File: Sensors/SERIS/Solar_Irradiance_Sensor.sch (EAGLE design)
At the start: 7 parts, among them IC1 LM324N, J1 ARDUINO_R3_SHIELD, U1 V_REG_317DPACK

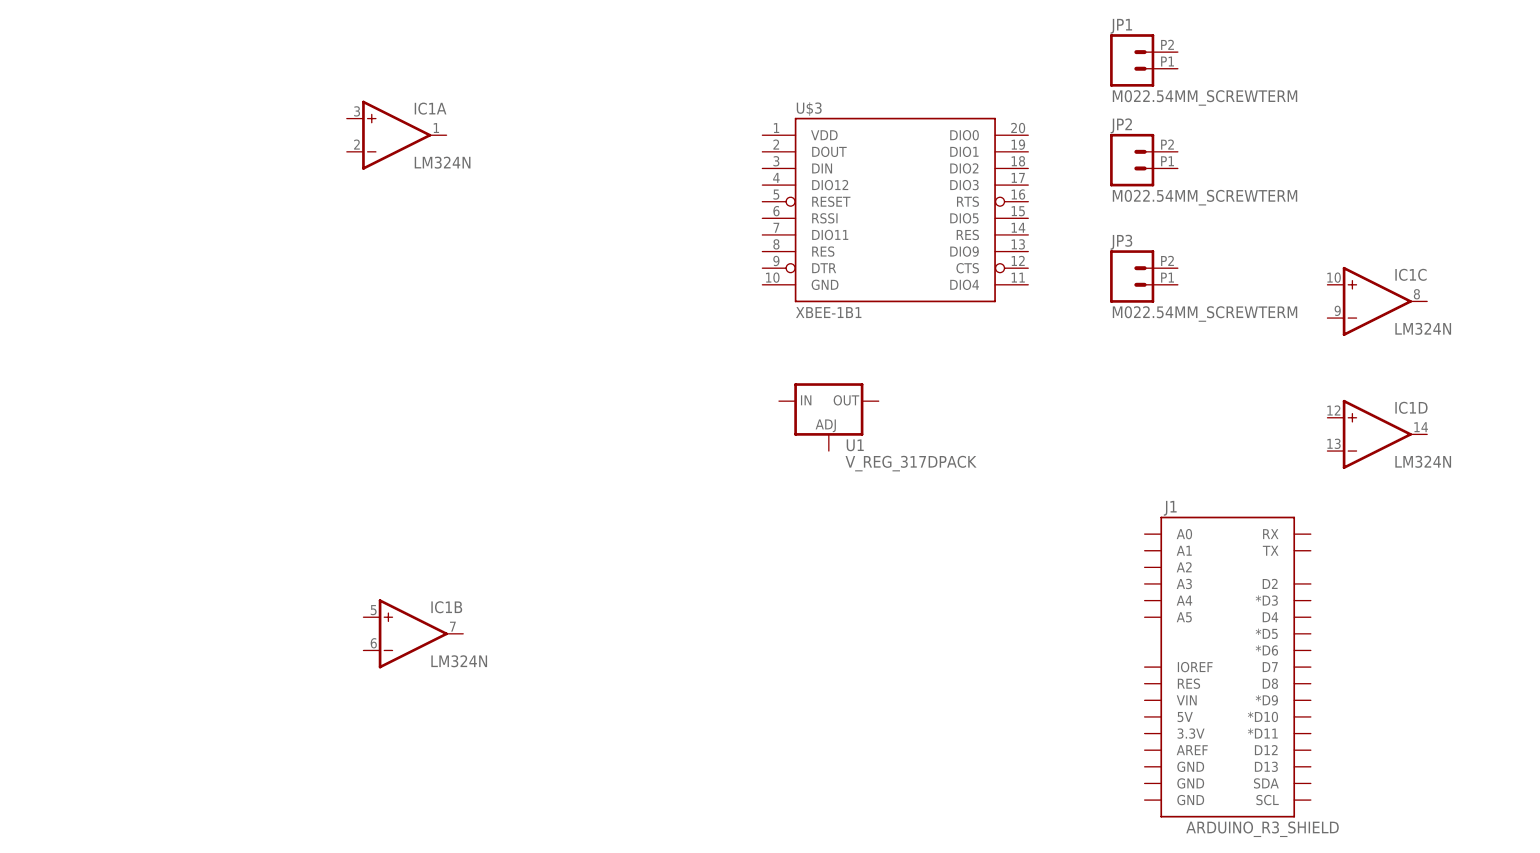
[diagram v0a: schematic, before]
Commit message: added various files (solar irradiance circuit)
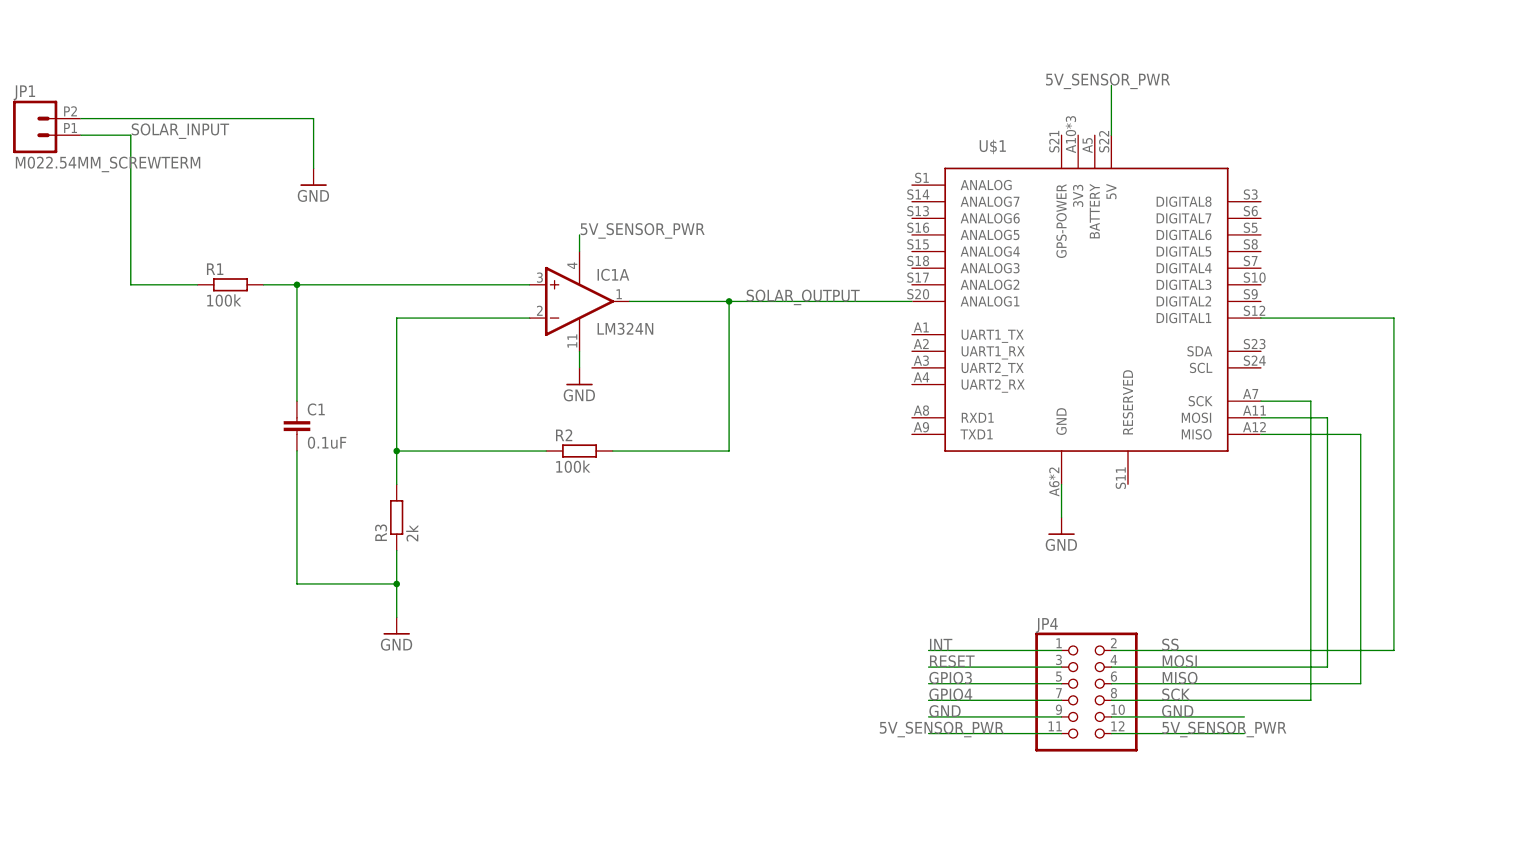
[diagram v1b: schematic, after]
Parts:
- removed J1: ARDUINO_R3_SHIELD, SparkFun-Boards:ARDUINO_R3_SHIELD
- removed JP2, JP3: M022.54MM_SCREWTERM, SparkFun-Connectors:M022.54MM_SCREWTERM
- removed U$3: XBEE-1B1, SparkFun-RF:XBEE-1B1
- removed U1: V_REG_317DPACK, SparkFun-PowerIC:V_REG_317DPACK
- added C1: 0.1uF, rcl:C-EU025-024X044
- added JP4: (no value), pinhead:PINHD-2X6
- added R1, R2: 100k, rcl:R-EU_0207/10
- added R3: 2k, rcl:R-EU_0207/10
- added U$1: WASP, wasp:WASP
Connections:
- new net 5V_SENSOR_PWR: IC1P.V+, JP4.11, JP4.12, U$1.5V
- new net GND: C1.2, IC1P.V-, JP1.2, JP4.10, JP4.9, R3.1, U$1.GND
- new net GPIO3: JP4.5
- new net GPIO4: JP4.7
- new net INT: JP4.1
- new net MISO: JP4.6, U$1.MISO
- new net MOSI: JP4.4, U$1.MOSI
- new net N$1: IC1A.-IN, R2.1, R3.2
- new net N$3: C1.1, IC1A.+IN, R1.2
- new net RESET: JP4.3
- new net SCK: JP4.8, U$1.SCK
- new net SOLAR_INPUT: JP1.1, R1.1
- new net SOLAR_OUTPUT: IC1A.OUT, R2.2, U$1.ANALOG1
- new net SS: JP4.2, U$1.DIGITAL1
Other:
- moved on the sheet: IC1A, JP1

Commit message: eagle circuit update SERIS
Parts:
- JP4: value (none) -> MAX31865
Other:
- moved on the sheet: C1, IC1A, JP1, JP4, R1, R2, R3, U$1

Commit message: .
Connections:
- removed net N$3: C1.1, IC1A.+IN, R1.2
- new net N$2: C1.1, IC1A.+IN, R1.2, U$1.ANALOG3
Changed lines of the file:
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@@
-</segment>
-</net>
-<net name="N$3" class="0">
-<segment>
-<pinref part="R1" gate="G$1" pin="2"/>
-<pinref part="IC1" gate="A" pin="+IN"/>
-<wire x1="43.18" y1="111.76" x2="48.26" y2="111.76" width="0.1524" layer="91"/>
-<pinref part="C1" gate="G$1" pin="1"/>
-<wire x1="48.26" y1="111.76" x2="83.82" y2="111.76" width="0.1524" layer="91"/>
-<wire x1="48.26" y1="93.98" x2="48.26" y2="111.76" width="0.1524" layer="91"/>
-<junction x="48.26" y="111.76"/>
 </segment>
 </net>
@@
 </segment>
 </net>
+<net name="N$2" class="0">
+<segment>
+<pinref part="R1" gate="G$1" pin="2"/>
+<pinref part="IC1" gate="A" pin="+IN"/>
+<wire x1="43.18" y1="111.76" x2="48.26" y2="111.76" width="0.1524" layer="91"/>
+<pinref part="C1" gate="G$1" pin="1"/>
+<wire x1="48.26" y1="111.76" x2="83.82" y2="111.76" width="0.1524" layer="91"/>
+<wire x1="48.26" y1="93.98" x2="48.26" y2="111.76" width="0.1524" layer="91"/>
+<junction x="48.26" y="111.76"/>
+<wire x1="132.08" y1="121.92" x2="48.26" y2="121.92" width="0.1524" layer="91"/>
+<wire x1="48.26" y1="121.92" x2="48.26" y2="111.76" width="0.1524" layer="91"/>
+<wire x1="132.08" y1="121.92" x2="132.08" y2="114.3" width="0.1524" layer="91"/>
+<pinref part="U$1" gate="G$1" pin="ANALOG3"/>
+<wire x1="132.08" y1="114.3" x2="142.24" y2="114.3" width="0.1524" layer="91"/>
+</segment>
+</net>
